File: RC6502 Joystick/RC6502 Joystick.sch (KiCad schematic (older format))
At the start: 44 parts, among them J1 Atari_Joystick, J2 Port, J3 Base, J4 RC6502_Backplane, SW1 SW_Push, SW2 SW_Push, SW3 SW_Push, SW4 SW_Push, SW5 SW_Push, SW6 SW_Push, SW7 SW_Push, SW8 SW_Push, U1 74LS245, U2 74LS373, U3 74LS138, U4 74LS138

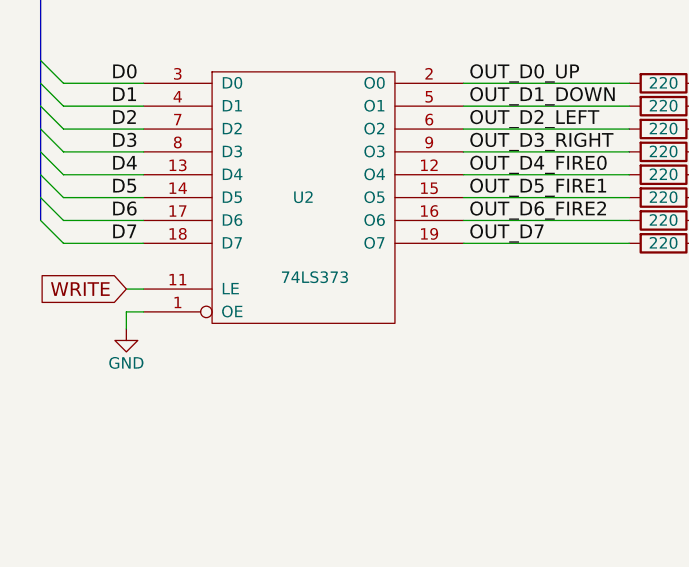
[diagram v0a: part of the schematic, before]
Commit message: Accidentally put 74LS373 instead of 74LS374
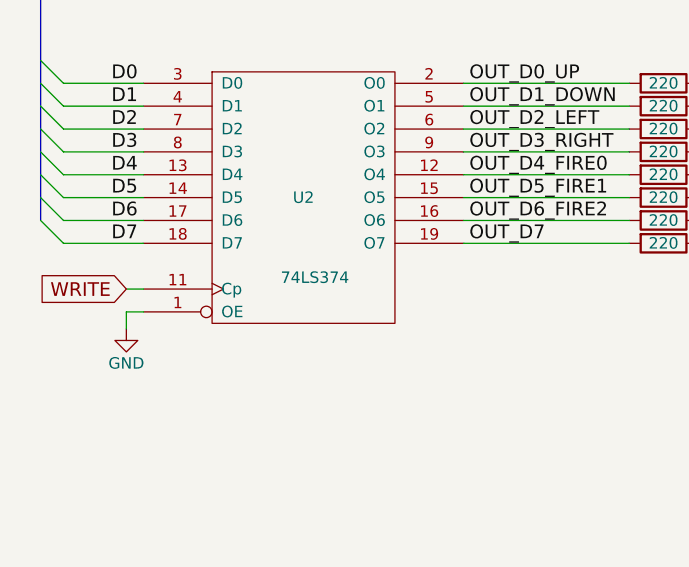
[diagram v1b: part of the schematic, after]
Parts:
- removed U2: 74LS373, Housings_DIP:DIP-20_W7.62mm_Socket, symbol 74LS373
- added U2: 74LS374, Housings_DIP:DIP-20_W7.62mm_Socket, symbol 74LS374
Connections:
- net D0: now also U2.3 (D0)
- net D1: now also U2.4 (D1)
- net D2: now also U2.7 (D2)
- net D3: now also U2.8 (D3)
- net D4: now also U2.13 (D4)
- net D5: now also U2.14 (D5)
- net D6: now also U2.17 (D6)
- net D7: now also U2.18 (D7)
- net GND: now also U2.1 (OE), U2.10 (GND)
- net OUT_D0_UP: now also U2.2 (O0)
- net OUT_D1_DOWN: now also U2.5 (O1)
- net OUT_D2_LEFT: now also U2.6 (O2)
- net OUT_D3_RIGHT: now also U2.9 (O3)
- net OUT_D4_FIRE0: now also U2.12 (O4)
- net OUT_D5_FIRE1: now also U2.15 (O5)
- net OUT_D6_FIRE2: now also U2.16 (O6)
- net OUT_D7: now also U2.19 (O7)
- net VCC: now also U2.20 (VCC)
- net WRITE: now also U2.11 (Cp)
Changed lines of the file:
@@
 Text GLabel 6975 875  1    60   Output ~ 0
 READ
-$Comp
-L 74LS373 U2
-U 1 1 5C237A24
-P 2125 4475
-F 0 "U2" H 2125 4475 50  0000 C CNN
-F 1 "74LS373" H 2175 4125 50  0000 C CNN
-F 2 "Housings_DIP:DIP-20_W7.62mm_Socket" H 2125 4475 50  0001 C CNN
-F 3 "" H 2125 4475 50  0001 C CNN
-	1    2125 4475
-	1    0    0    -1
-$EndComp
 Entry Wire Line
 	1075 4675 975  4575
@@
 Text Notes 7025 6875 0    60   ~ 0
 Sort of a mish-mash digital I/O module, with a DB9 connector for use with Atari-style\njoysticks. Matches address decoding used by PSG so that they can coincide within the\nsame 4K address space.
+$Comp
+L 74LS374 U2
+U 1 1 5C7C91B5
+P 2125 4475
+F 0 "U2" H 2125 4475 50  0000 C CNN
+F 1 "74LS374" H 2175 4125 50  0000 C CNN
+F 2 "Housings_DIP:DIP-20_W7.62mm_Socket" H 2125 4475 50  0001 C CNN
+F 3 "" H 2125 4475 50  0001 C CNN
+	1    2125 4475
+	1    0    0    -1
+$EndComp
 $EndSCHEMATC
